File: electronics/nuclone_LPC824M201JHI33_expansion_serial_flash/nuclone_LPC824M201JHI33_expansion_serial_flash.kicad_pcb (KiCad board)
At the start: 2 copper layers, 45.8 x 25.5 mm, 5 parts, among them J1 nuclone_small_left, J2 nuclone_small_right

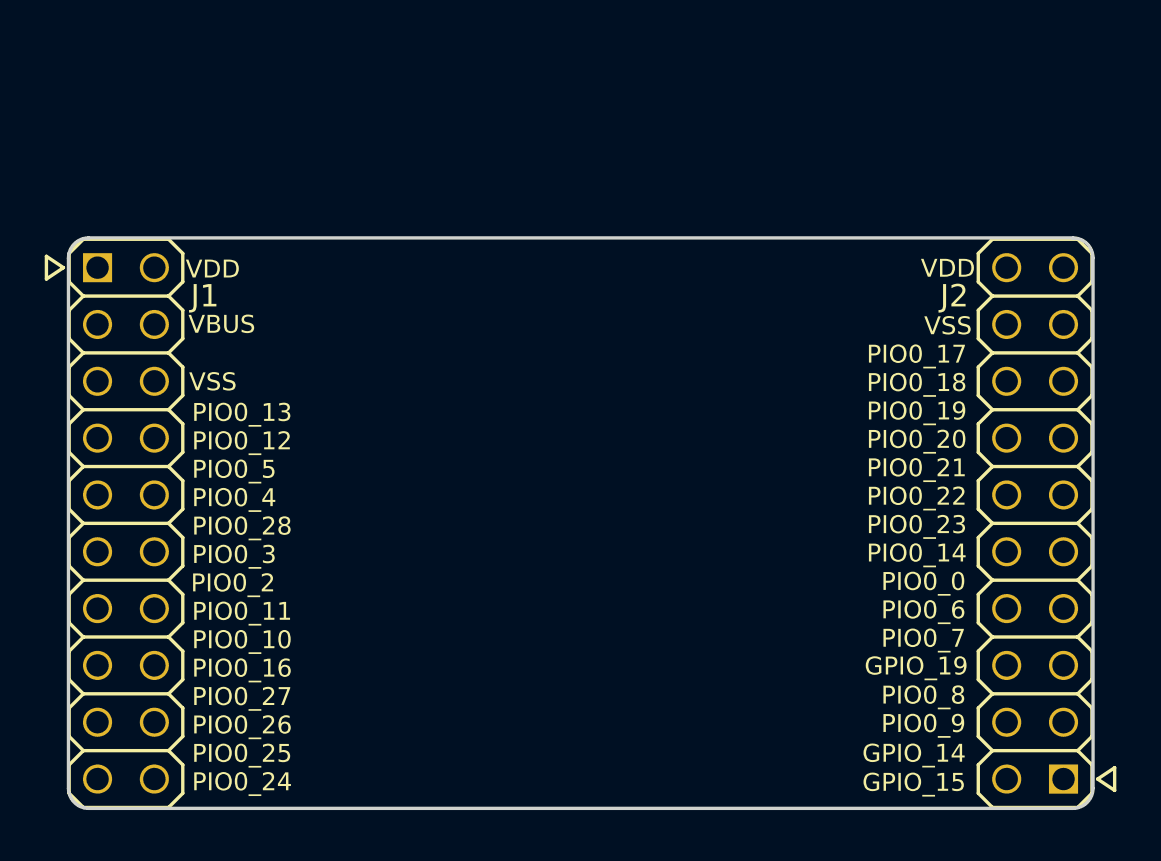
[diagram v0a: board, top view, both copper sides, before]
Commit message: routed UART connection
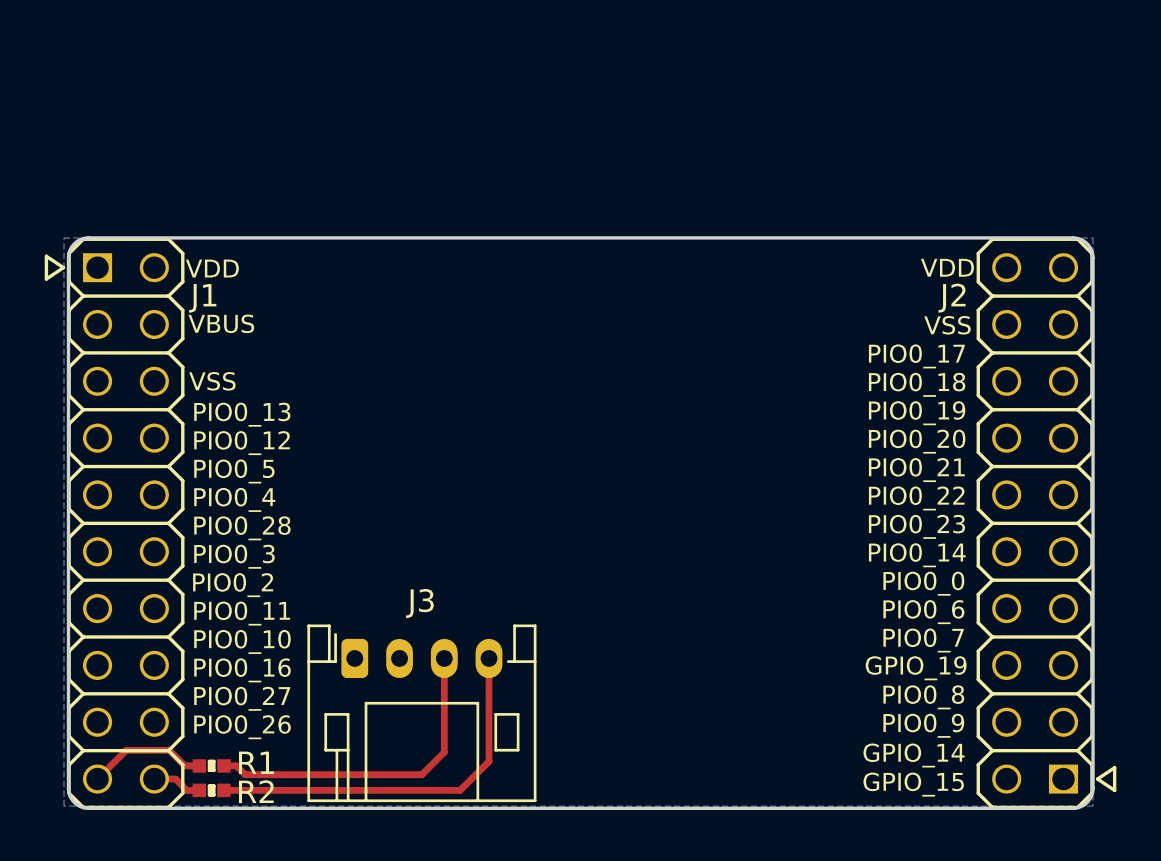
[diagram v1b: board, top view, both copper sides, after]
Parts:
- added J3: DevBoardUartInput, Connector_JST:JST_PH_S4B-PH-K_1x04_P2.00mm_Horizontal, F.Cu at (75.0, 92.4)
- added R1: 100, SquantorRcl:R_0402_hand, F.Cu at (68.6, 97.2)
- added R2: 100, SquantorRcl:R_0402_hand, F.Cu at (68.6, 98.3)
- moved N1 7.90 mm to (93.3, 92.0)
- moved N2 7.90 mm to (91.8, 96.0)
- moved N3 7.90 mm to (94.1, 98.0)
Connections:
- J1 pad 19: /PIO0_25 -> /UART_RX
- J1 pad 20: /PIO0_24 -> /UART_TX
- J2 pad 1: /GPIO_14 -> /GPIO_15
- J2 pad 2: /GPIO_15 -> /GPIO_14
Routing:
- net Net-(J3-Pad4): track 0.00 -> 17.0 mm
- net Net-(J3-Pad3): track 0.00 -> 14.6 mm
- net /UART_RX: track 0.00 -> 5.37 mm
- net /UART_TX: track 0.00 -> 2.22 mm
- added copper zone on B.Cu, net /VSS
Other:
- board text removed: "PIO0_24"
- board text removed: "PIO0_25"

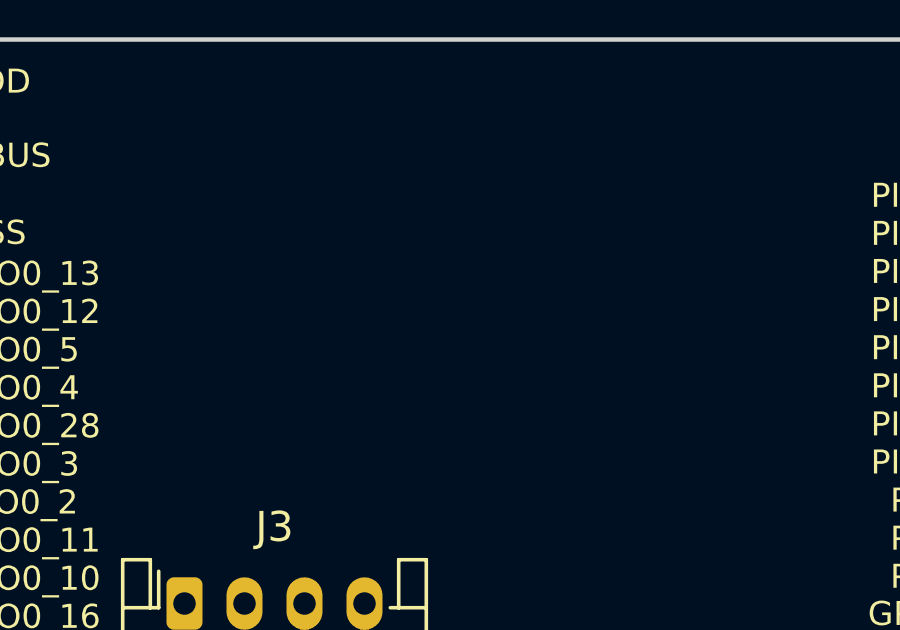
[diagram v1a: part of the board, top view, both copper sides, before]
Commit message: imported initial components of the SPI flash chip
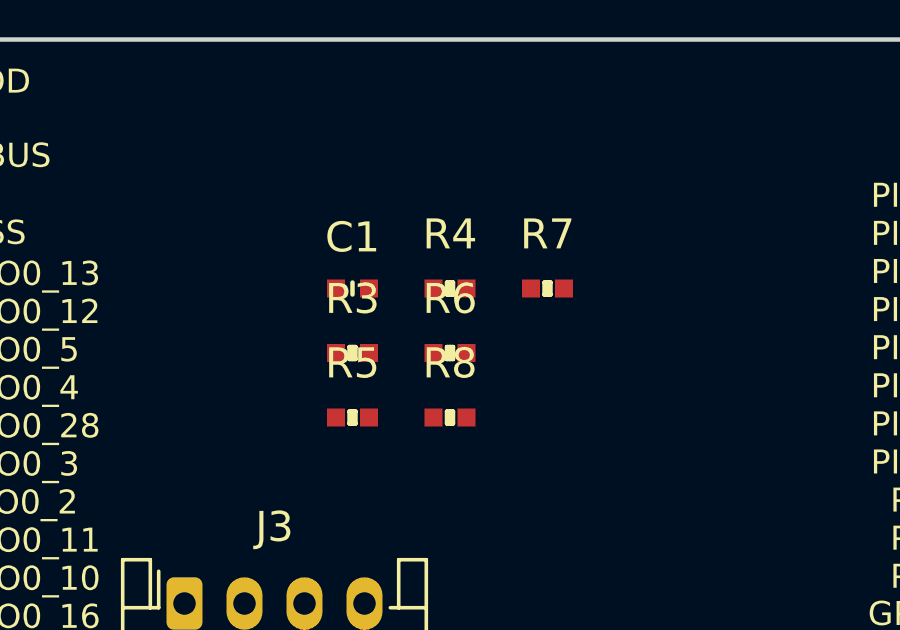
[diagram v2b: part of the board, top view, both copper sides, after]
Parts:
- added C1: 1u, SquantorRcl:C_0402, F.Cu at (80.6, 81.9)
- added R3: 100, SquantorRcl:R_0402_hand, F.Cu at (80.6, 84.0)
- added R4: 100, SquantorRcl:R_0402_hand, F.Cu at (83.8, 81.9)
- added R5: 10k, SquantorRcl:R_0402_hand, F.Cu at (80.6, 86.2)
- added R6: 10k, SquantorRcl:R_0402_hand, F.Cu at (83.8, 84.0)
- added R7: 100, SquantorRcl:R_0402_hand, F.Cu at (87.1, 81.9)
- added R8: 100, SquantorRcl:R_0402_hand, F.Cu at (83.8, 86.2)
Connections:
- J1 pad 11: /PIO0_28 -> /CE_FLASH
- J1 pad 16: /PIO0_16 -> /SPI_CLK
- J1 pad 17: /PIO0_27 -> /SPI_CIPO
- J1 pad 18: /PIO0_26 -> /SPI_COPI

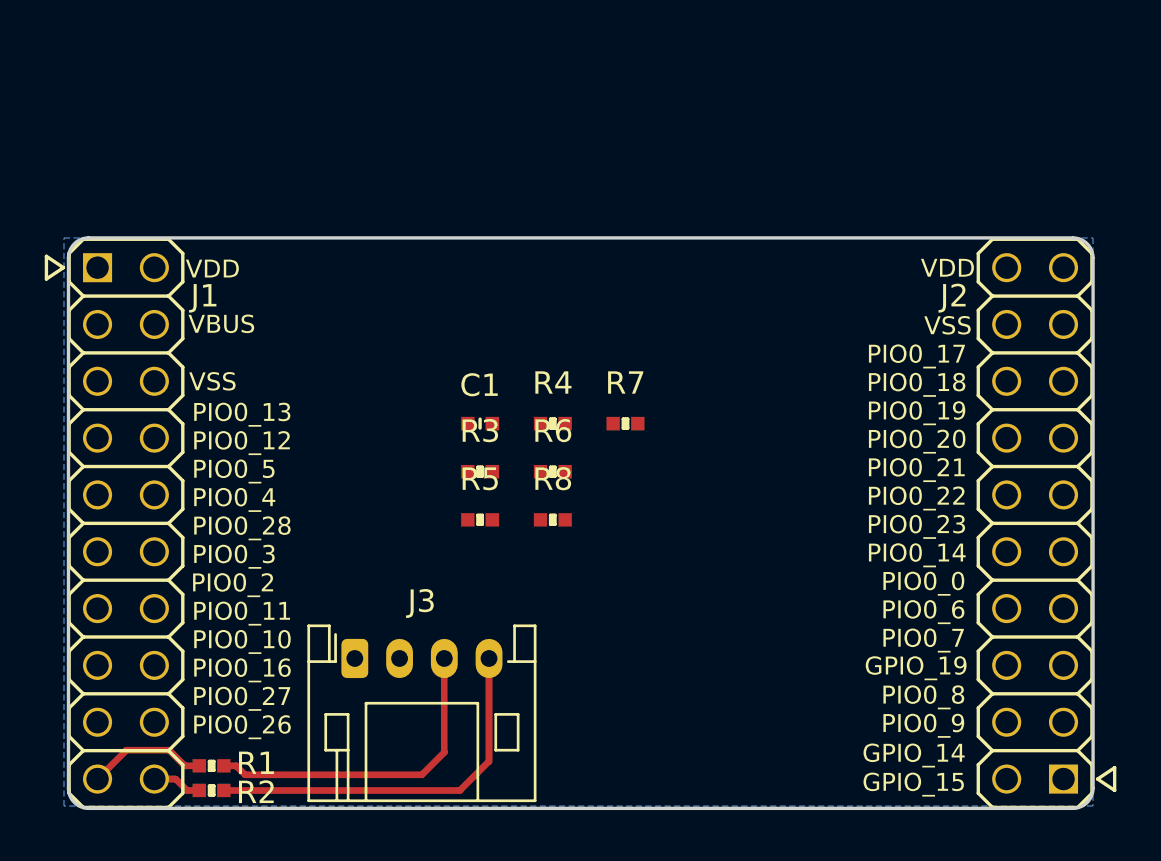
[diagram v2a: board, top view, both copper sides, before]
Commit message: initial placement and some beginning of routing, but need to make it more compact
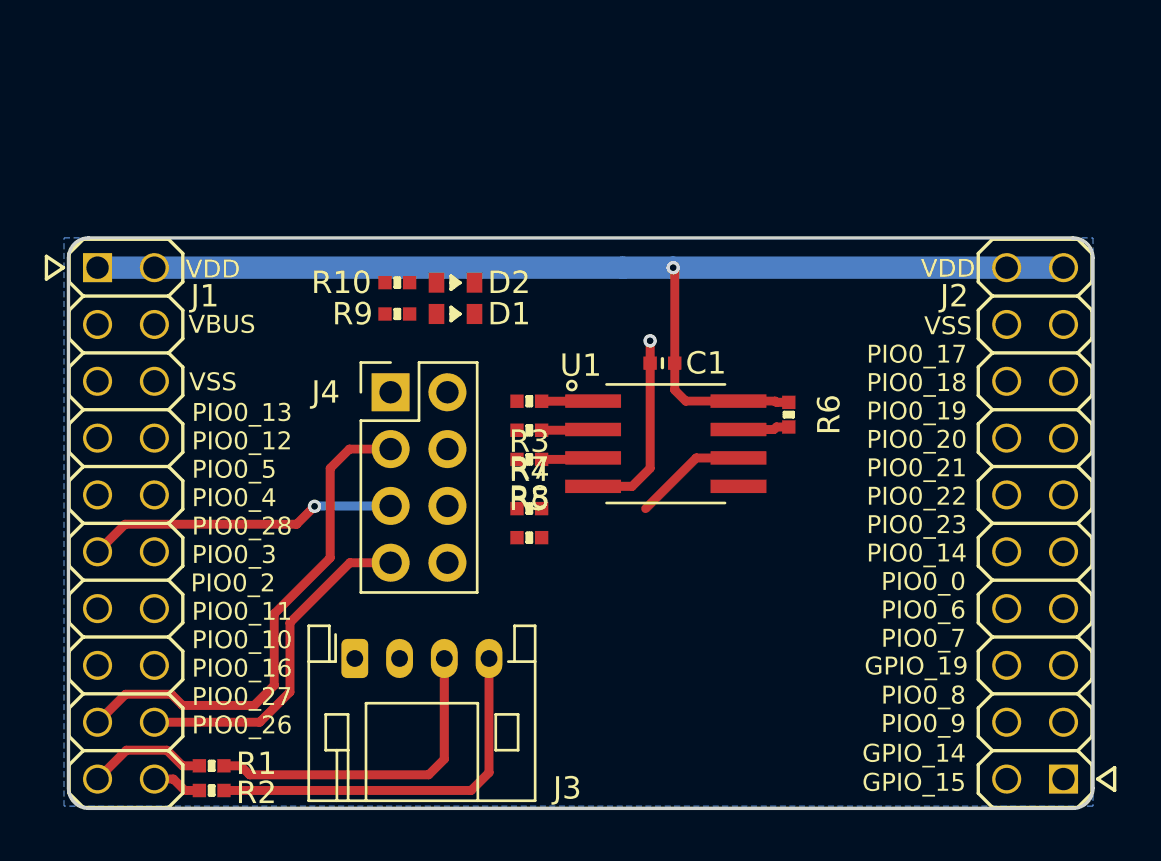
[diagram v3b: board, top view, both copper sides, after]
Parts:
- added D1: LED, SquantorDiodes:LED_0603_hand, F.Cu at (79.5, 77.0)
- added D2: LED, SquantorDiodes:LED_0603_hand, F.Cu at (79.5, 75.6)
- added J4: Conn_02x04_Odd_Even, Connector_PinHeader_2.54mm:PinHeader_2x04_P2.54mm_Vertical, F.Cu at (76.6, 80.5)
- added R10: 4.7K, SquantorRcl:R_0402_hand, F.Cu at (76.9, 75.6)
- added R9: 4.7K, SquantorRcl:R_0402_hand, F.Cu at (76.9, 77.0)
- added U1: generic 25XNN serial flash, SquantorIC:SOIC-8_dual_wide, F.Cu at (88.9, 82.8)
- moved R6 10.9 mm to (94.4, 81.5), turned to 270 degrees
- moved C1 8.59 mm to (88.8, 79.2), turned to 180 degrees
- moved R7 5.74 mm to (82.8, 85.7)
- moved R3 3.84 mm to (82.8, 80.9), turned to 180 degrees
- moved R5 3.48 mm to (82.8, 83.5), turned to 180 degrees
- moved R8 1.32 mm to (82.8, 87.0)
- moved R4 1.09 mm to (82.8, 82.2), turned to 180 degrees
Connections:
- J1 pad 11: /CE_FLASH -> /SPI_CLK
- J1 pad 16: /SPI_CLK -> /CE_FLASH
- J3 pad 2: /VDD -> /VBUS
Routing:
- net /VDD: track 0.00 -> 54.0 mm, vias 0 -> 1
- net /SPI_CIPO: track 0.00 -> 22.8 mm
- net /SPI_COPI: track 0.00 -> 15.3 mm
- net /SPI_CLK: track 0.00 -> 13.9 mm, vias 0 -> 1
- net /VSS: track 0.00 -> 8.58 mm, vias 0 -> 1
- net Net-(R7-Pad2): track 0.00 -> 5.09 mm
- net Net-(R5-Pad1): track 0.00 -> 2.33 mm
- net Net-(R4-Pad1): track 0.00 -> 2.31 mm
- net Net-(R3-Pad1): track 0.00 -> 2.30 mm
- net Net-(R6-Pad2): track 0.00 -> 2.30 mm

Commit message: WIP placement
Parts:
- added R11: 100, SquantorRcl:R_0402_hand, F.Cu at (79.0, 88.4)
- added R12: 100, SquantorRcl:R_0402_hand, F.Cu at (77.6, 76.6)
- J4: value Conn_02x04_Odd_Even -> Conn_02x06_Odd_Even; footprint Connector_PinHeader_2.54mm:PinHeader_2x04_P2.54mm_Vertical -> Connector_PinHeader_2.54mm:PinHeader_2x06_P2.54mm_Vertical
- moved R6 18.8 mm to (76.3, 76.6)
- moved J4 16.4 mm to (93.0, 79.6)
- moved C1 14.5 mm to (74.7, 82.7), turned to 270 degrees
- moved R8 10.7 mm to (80.2, 76.6), turned to 270 degrees
- moved U1 10.6 mm to (78.3, 82.5), turned to 90 degrees
- moved R10 10.00 mm to (74.1, 66.0)
- moved R9 10.00 mm to (74.1, 67.4)
- moved D1 10.00 mm to (76.7, 67.4)
- moved D2 10.00 mm to (76.7, 66.0)
- moved R7 9.90 mm to (78.9, 76.6), turned to 270 degrees
- moved R3 9.86 mm to (76.4, 88.4), turned to 270 degrees
- moved R4 8.03 mm to (77.7, 88.4), turned to 270 degrees
- moved R5 5.50 mm to (80.3, 88.4), turned to 270 degrees
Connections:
- net /PIO0_12 renamed /LED0
- net /PIO0_13 renamed /LED1
- J1 pad 11: /SPI_CLK -> /PIO0_28
- J1 pad 16: /CE_FLASH -> /PIO0_16
- J1 pad 17: /SPI_CIPO -> /PIO0_27
- J1 pad 18: /SPI_COPI -> /PIO0_26
- J1 pad 3: /VBUS -> Net-(J1-Pad3)
- J1 pad 5: /VSS -> Net-(J1-Pad5)
- J2 pad 11: /PIO0_21 -> /CE_FLASH
- J2 pad 12: /PIO0_22 -> /CLK
- J2 pad 13: /PIO0_19 -> /SIO2
- J2 pad 14: /PIO0_20 -> /SIO3
- J2 pad 15: /PIO0_17 -> /SIO0
- J2 pad 16: /PIO0_18 -> /SIO1
- J2 pad 17: /VSS -> Net-(J2-Pad17)
- J2 pad 19: /VDD -> Net-(J2-Pad19)
- J4 pad 3: /SPI_CIPO -> /CLK
- J4 pad 5: /SPI_CLK -> /SIO0
- J4 pad 7: /SPI_COPI -> /SIO1
- R4 pad 2: /SPI_CIPO -> /SIO1
- R7 pad 1: /SPI_CLK -> /CLK
- R8 pad 1: /SPI_COPI -> /SIO0
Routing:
- net /SPI_CIPO: track 22.8 -> 0.00 mm
- net /SPI_COPI: track 15.3 -> 0.00 mm
- net /SPI_CLK: track 13.9 -> 0.00 mm, vias 1 -> 0
- net /VDD: track 54.0 -> 43.2 mm, vias 1 -> 0
- net /VSS: track 8.58 -> 0.00 mm, vias 1 -> 0
- net Net-(R7-Pad2): track 5.09 -> 0.00 mm
- net Net-(R11-Pad1): track 2.33 -> 0.00 mm
- net Net-(R4-Pad1): track 2.31 -> 0.00 mm
- net Net-(R3-Pad1): track 2.30 -> 0.00 mm
- net Net-(R12-Pad2): track 2.30 -> 0.00 mm

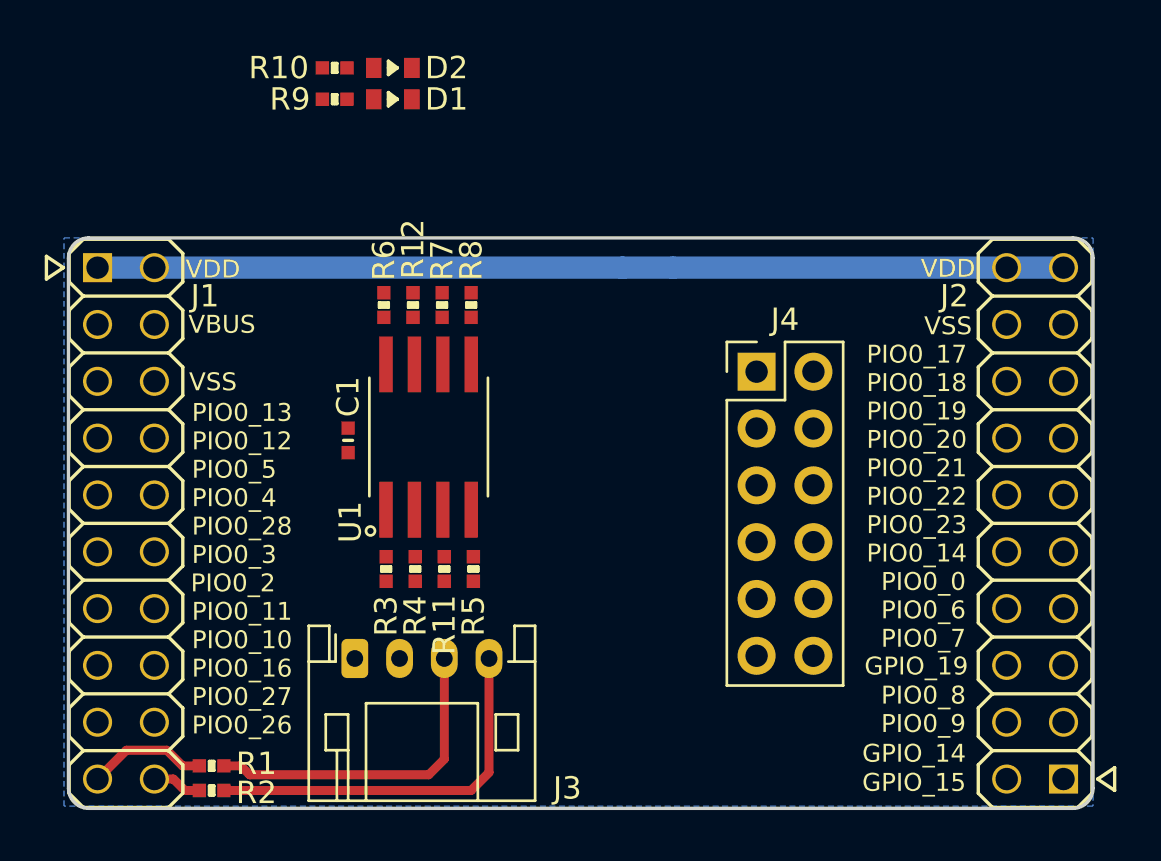
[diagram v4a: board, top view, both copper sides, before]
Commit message: routed flash chip and the QSPI debug connector, WIP silk placement
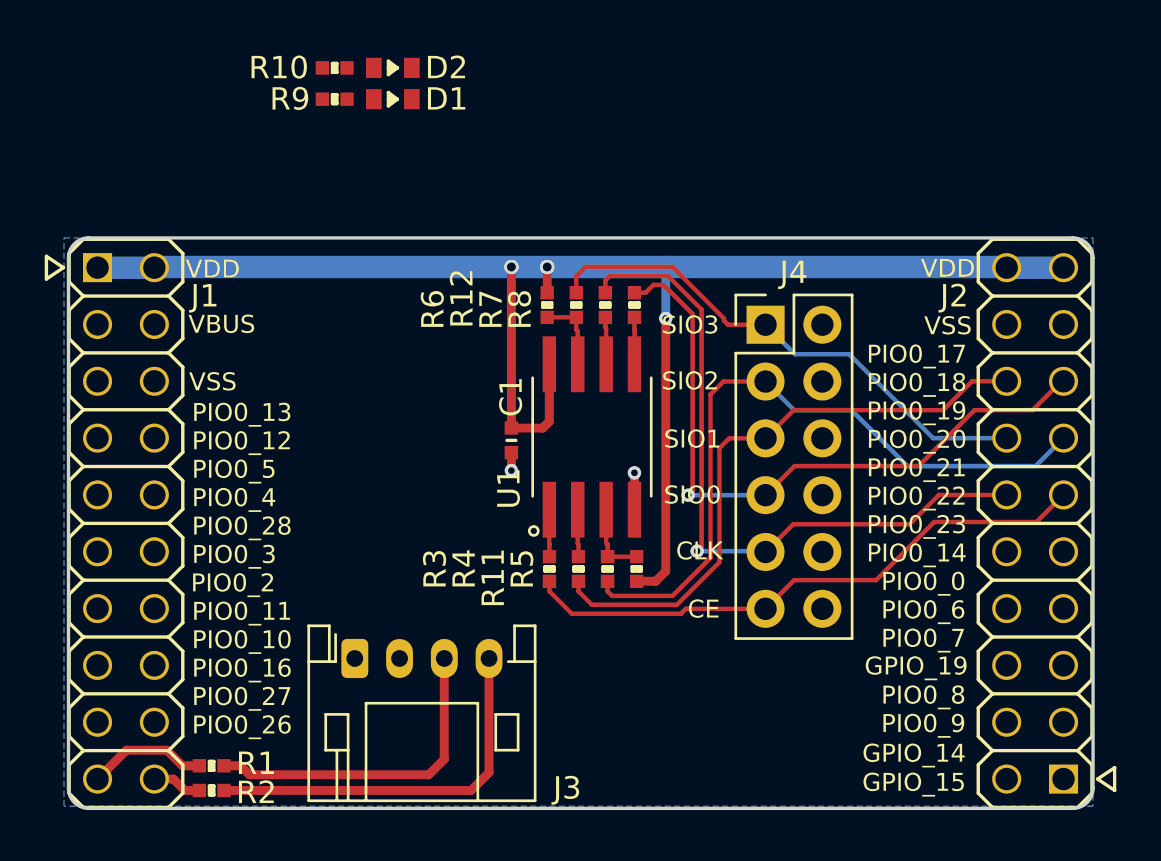
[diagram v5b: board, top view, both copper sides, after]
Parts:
- moved N2 15.1 mm to (76.7, 95.3)
- moved N3 15.1 mm to (79.0, 97.3)
- moved N1 7.34 mm to (86.8, 95.4)
- moved R12 7.30 mm to (84.9, 76.6)
- moved C1 7.30 mm to (82.0, 82.7)
- moved R11 7.30 mm to (86.3, 88.4)
- moved R3 7.30 mm to (83.7, 88.4)
- moved R4 7.30 mm to (85.0, 88.4)
- moved R5 7.30 mm to (87.6, 88.4)
- moved R6 7.30 mm to (83.6, 76.6)
- moved R7 7.30 mm to (86.2, 76.6)
- moved R8 7.30 mm to (87.5, 76.6)
- moved U1 7.30 mm to (85.6, 82.5)
- moved J4 2.14 mm to (93.4, 77.5)
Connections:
- J4 pad 1: /CE_FLASH -> /SIO3
- J4 pad 11: /SIO3 -> /CE_FLASH
- J4 pad 3: /CLK -> /SIO2
- J4 pad 5: /SIO0 -> /SIO1
- J4 pad 7: /SIO1 -> /SIO0
- J4 pad 9: /SIO2 -> /CLK
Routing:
- net /CLK: track 0.00 -> 31.3 mm, vias 0 -> 1
- net /SIO2: track 0.00 -> 31.2 mm
- net /SIO0: track 0.00 -> 30.4 mm, vias 0 -> 1
- net /VDD: track 43.2 -> 71.0 mm, vias 0 -> 3
- net /SIO1: track 0.00 -> 27.0 mm
- net /CE_FLASH: track 0.00 -> 26.0 mm
- net /SIO3: track 0.00 -> 23.4 mm
- net Net-(R12-Pad2): track 0.00 -> 3.43 mm
- net Net-(R11-Pad1): track 0.00 -> 3.43 mm
- net /VSS: track 0.00 -> 2.45 mm, vias 0 -> 2
- net Net-(R4-Pad1): track 0.00 -> 2.11 mm
- net Net-(R7-Pad2): track 0.00 -> 2.11 mm
- net Net-(R3-Pad1): track 0.00 -> 2.10 mm
- net Net-(R8-Pad2): track 0.00 -> 2.10 mm
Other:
- board text added: "CE"
- board text added: "CLK"
- board text added: "SIO0"
- board text added: "SIO1"
- board text added: "SIO2"
- board text added: "SIO3"
